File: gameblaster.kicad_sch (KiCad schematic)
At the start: 67 parts, among them IC1 TEA2025, IC10 74LS138, IC11 74LS08, IC12 74LS14, IC2 SAA1099, IC3 SAA1099, IC4 74LS374, IC5 74LS138, IC6 74LS74, IC7 74LS245, IC8 74LS32, IC9 74LS125, J1 Conn_02x06_Odd_Even

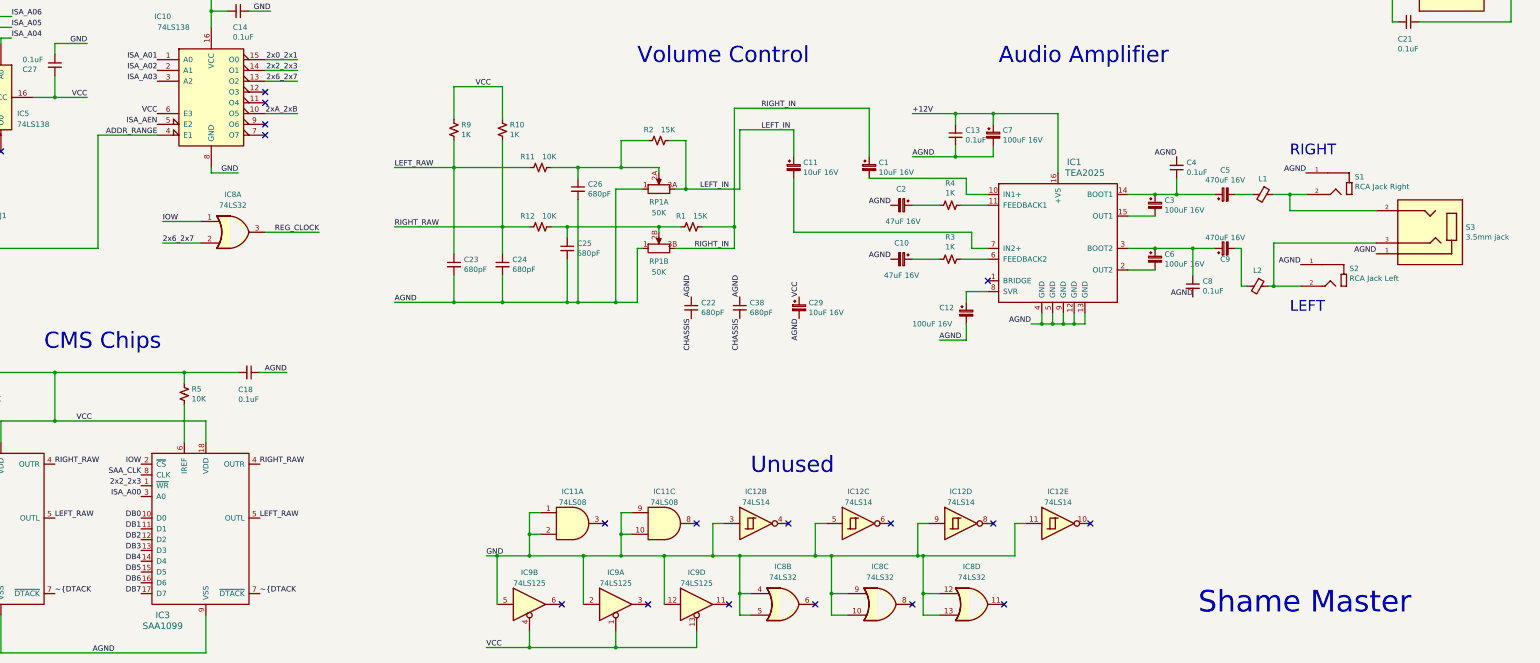
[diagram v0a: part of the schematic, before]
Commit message: add zener regulator for SAA1099s
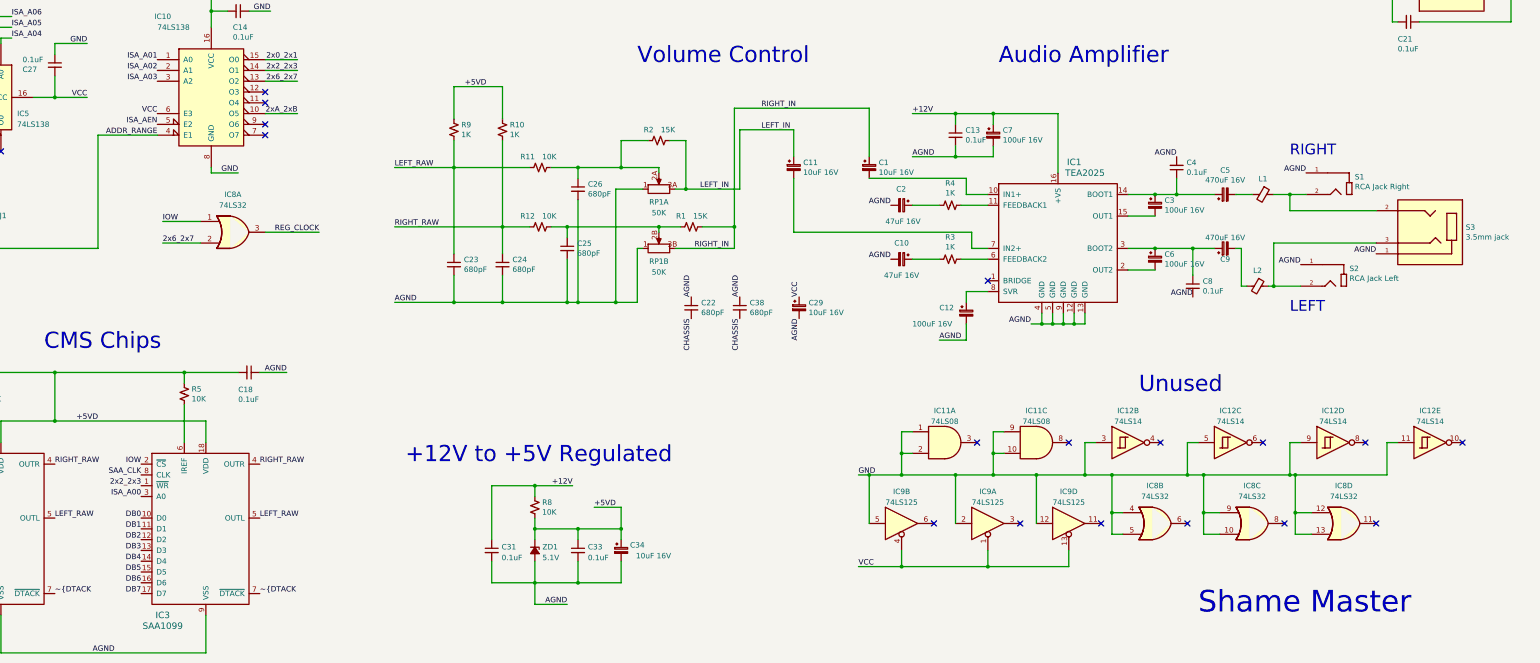
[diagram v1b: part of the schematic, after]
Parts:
- added C31, C33: 0.1uF, gameblaster:CAPAC200, symbol Device:C_Small
- added C34: 10uF 16V, gameblaster:CAPAP100, symbol gameblaster-rescue:CP_Small-Device
- added R8: 10K, gameblaster:RESA400, symbol Device:R_Small_US
- added ZD1: 5.1V, gameblaster:DIOA400, symbol Device:D_Zener_Small_Filled
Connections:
- net +12V: now also C31.1, R8.1
- net AGND: now also C31.2, C33.2, C34.2, ZD1.2 (A)
- net VCC: no longer C18.2, C19.1, IC2.18 (VDD), IC3.18 (VDD), R10.1, R5.1, R7.1, R9.1
- new net +5VD: C18.2, C19.1, C33.1, C34.1, IC2.18 (VDD), IC3.18 (VDD), R10.1, R5.1, R7.1, R8.2, R9.1, ZD1.1 (K)
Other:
- note added: "+12V to +5V Regulated"
- moved on the sheet: IC11A, IC11C, IC12B, IC12C, IC12D, IC12E, IC8B, IC8C, IC8D, IC9A, IC9B, IC9D

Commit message: add logo, engorge zones, clip solder mask from card fingers
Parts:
- S2: footprint gameblaster:CUI_RCJ-042 -> gameblaster:CUI_RCJ-043
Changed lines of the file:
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@@
       (effects (font (size 1.27 1.27)) (justify right))
     )
-    (property "Footprint" "gameblaster:CUI_RCJ-042" (id 2) (at 355.6 184.15 0)
+    (property "Footprint" "gameblaster:CUI_RCJ-043" (id 2) (at 355.6 184.15 0)
       (effects (font (size 1.27 1.27)) hide)
     )
@@
     )
     (path "/00000000-0000-0000-0000-000063df565c"
-      (reference "S2") (unit 1) (value "RCA Jack Left") (footprint "gameblaster:CUI_RCJ-042")
+      (reference "S2") (unit 1) (value "RCA Jack Left") (footprint "gameblaster:CUI_RCJ-043")
     )
     (path "/00000000-0000-0000-0000-000063df6ee7"

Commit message: so much dumb shit
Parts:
- removed C17: 0.1uF, gameblaster:CAPAC200, symbol gameblaster-rescue:C_Small-Adlib-cache
- removed C23, C24: 680pF, gameblaster:CAPAC200, symbol gameblaster-rescue:C_Small-Adlib-cache
- removed IC12: 74LS14, gameblaster:DIP254P762X635-14, symbol 74xx:74LS14
- removed R10, R9: 1K, gameblaster:RESA400, symbol Device:R_Small_US
- added C35: 0.1uF?, gameblaster:CAPAC200, symbol Device:C_Small
- added C? (x2): 1uF tant, gameblaster:CAPAP100, symbol Device:C_Polarized_Small
- added R?: 10K, gameblaster:RESA400, symbol Device:R_Small_US
- C10, C2: value 47uF 16V -> 22uF 16V
- R6: value 4.7K -> 1K
- R8: value 10K -> 470R
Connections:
- net +12V: no longer C13.1, C7.1, IC1.16 (+VS)
- net GND: now also C35.2, R?.2; no longer IC11.1, IC11.2, IC9.2, IC9.5
- net ISA_RST: now also C37.2, IC9.4
- net LEFT_IN: now also C11.2, RP1.2A; no longer C11.1, RP1.3A
- net RIGHT_IN: now also C1.2, RP1.2B; no longer C1.1, RP1.3B
- net VCC: now also IC11.1, IC9.2; no longer C37.2, IC9.1, IC9.4
- net ~{DTACK}: now also IC9.5; no longer IC11.4
- net ~{2x6_2x7}: now reaches IC10.12 (O3)
- net ~{2x6_2x7}: now also IC8.2
- net at IC1.10 (IN1+): now also C1.1; no longer C1.2
- net at IC1.7 (IN2+): now also C11.1; no longer C11.2
- net at C26.1, R11.2: now also C?.1; no longer R2.1, RP1.2A
- net at C25.1, R12.2: now also C?.1; no longer R1.1, RP1.2B
- net at IC6.10 (~{S}): now also IC9.6; no longer IC11.6
- net at IC6.11 (C): now also IC9.3, R?.1
- net ~{SAA_IOW}: now reaches IC11.3
- net ~{SAA_IOW}: now also IC2.1 (~{WR}), IC3.1 (~{WR}), C35.1
- net +5VD renamed +5VA
- net +5VA: now also C13.1, C7.1, IC1.16 (+VS)
- net 2x0_2x1 renamed ~{2x0_2x1}
- net ~{2x0_2x1}: now also IC11.12, IC2.2 (~{CS}); no longer IC2.1 (~{WR})
- net 2x2_2x3 renamed ~{2x2_2x3}
- net ~{2x2_2x3}: now also IC11.13, IC3.2 (~{CS}); no longer IC3.1 (~{WR})
- removed net 2x6_2x7: IC10.13 (O2), IC11.12, IC8.2
- net 2xA_2xB renamed ~{2xA_2xB}
- net ~{2xA_2xB}: no longer IC11.13
- net ADDR_RANGE renamed ~{ADDR_RANGE}
- net IOR renamed ~{IOR}
- net IOW renamed ~{IOW}
- net ~{IOW}: now also IC11.2, IC9.1; no longer IC2.2 (~{CS}), IC3.2 (~{CS})
- net REG_CLOCK renamed ~{REG_CLOCK}
- net ~{RESET}: no longer names the net of IC11.5
- new net: C?.2, R1.1, RP1.3B
- new net: C?.2, R2.1, RP1.3A
- new net ~{7FH_READ}: IC10.13 (O2)
- no-connect marks 52 -> 45
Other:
- note added: "(Leave RP1 unpopulated and replace R1 and R2 with 4.7K resistors for a fixed "medium" volume)"
- note added: "Write Logic"
- moved on the sheet: C1, C11, C20, C25, C26, C28, C37, IC11A, IC11B, IC11D, IC4, IC6A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

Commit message: dumb schematic shit
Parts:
- gave numbers to parts that had none: 3
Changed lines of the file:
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@@
   (symbol (lib_id "Device:C_Polarized_Small") (at 181.61 172.72 90) (unit 1)
     (in_bom yes) (on_board yes) (fields_autoplaced)
-    (property "Reference" "C?" (id 0) (at 181.0639 167.6232 90))
+    (property "Reference" "C23" (id 0) (at 181.0639 167.6232 90))
     (property "Value" "1uF tant" (id 1) (at 181.0639 170.1601 90))
     (property "Footprint" "gameblaster:CAPAP100" (id 2) (at 181.61 172.72 0)
@@
   (symbol (lib_id "Device:C_Polarized_Small") (at 181.61 158.75 90) (unit 1)
     (in_bom yes) (on_board yes) (fields_autoplaced)
-    (property "Reference" "C?" (id 0) (at 181.0639 153.6532 90))
+    (property "Reference" "C17" (id 0) (at 181.0639 153.6532 90))
     (property "Value" "1uF tant" (id 1) (at 181.0639 156.1901 90))
     (property "Footprint" "gameblaster:CAPAP100" (id 2) (at 181.61 158.75 0)
@@
   (symbol (lib_id "Device:R_Small_US") (at 218.44 78.74 0) (unit 1)
     (in_bom yes) (on_board yes)
-    (property "Reference" "R?" (id 0) (at 220.98 77.47 0))
+    (property "Reference" "R9" (id 0) (at 220.98 77.47 0))
     (property "Value" "10K" (id 1) (at 219.71 80.01 0)
       (effects (font (size 1.27 1.27)) (justify left))
@@
       (reference "C16") (unit 1) (value "0.1uF") (footprint "gameblaster:CAPAC200")
     )
+    (path "/c08901b8-33b1-4c09-abd5-c90fae277cfd"
+      (reference "C17") (unit 1) (value "1uF tant") (footprint "gameblaster:CAPAP100")
+    )
     (path "/00000000-0000-0000-0000-000063e0a803"
       (reference "C18") (unit 1) (value "0.1uF") (footprint "gameblaster:CAPAC200")
@@
       (reference "C22") (unit 1) (value "680pF") (footprint "gameblaster:CAPAC200")
     )
+    (path "/04e1ceed-18cf-4d16-a60e-8b84fb42586e"
+      (reference "C23") (unit 1) (value "1uF tant") (footprint "gameblaster:CAPAP100")
+    )
     (path "/00000000-0000-0000-0000-00006403d753"
       (reference "C25") (unit 1) (value "680pF") (footprint "gameblaster:CAPAC200")
@@
       (reference "C38") (unit 1) (value "680pF") (footprint "gameblaster:CAPAC200")
     )
-    (path "/04e1ceed-18cf-4d16-a60e-8b84fb42586e"
-      (reference "C?") (unit 1) (value "1uF tant") (footprint "gameblaster:CAPAP100")
-    )
-    (path "/c08901b8-33b1-4c09-abd5-c90fae277cfd"
-      (reference "C?") (unit 1) (value "1uF tant") (footprint "gameblaster:CAPAP100")
-    )
     (path "/00000000-0000-0000-0000-000063e2477d"
       (reference "F1") (unit 1) (value "MountingHole") (footprint "gameblaster:MNT_KEYSTONE_9202")
@@
       (reference "R8") (unit 1) (value "470R") (footprint "gameblaster:RESA400")
     )
+    (path "/de5081d7-c9ca-401c-b128-a39de91cb81e"
+      (reference "R9") (unit 1) (value "10K") (footprint "gameblaster:RESA400")
+    )
     (path "/00000000-0000-0000-0000-000063dfd8aa"
       (reference "R11") (unit 1) (value "10K") (footprint "gameblaster:RESA400")
@@
       (reference "R19") (unit 1) (value "4.7K") (footprint "gameblaster:RESA400")
     )
-    (path "/de5081d7-c9ca-401c-b128-a39de91cb81e"
-      (reference "R?") (unit 1) (value "10K") (footprint "gameblaster:RESA400")
-    )
     (path "/1bd276f5-593a-4fdb-b158-a8c28f21f786"

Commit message: heavily annotate schematic
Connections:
- net AGND: now also C38.2; no longer C38.1
- net CHASSIS: now also C38.1; no longer C38.2
- net GND: now also IC11.4, IC11.5
- net ISA_IO_CH_RDY renamed ~{IORDY}
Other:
- note added: ""EMI" "Protection""
- note added: "+5V is low for a TEA2025B, but apparently still in operating range. (The Sound Blaster used a 12V -> 9V regulator, but the Game Blaster just used this zener-regulated 12V -> 5V circuit for all the analog power)"
- note added: "- ~{CS} goes low -> ~{WR} goes low - register 0/1 (control/data) selected by A0 - SAA1099 latches data from D0-D7 into register - SAA1099 pulls ~{DTACK} low when data trasnfer is complete"
- note added: "210"
- note added: "220"
- note added: "230"
- note added: "240"
- note added: "250"
- note added: "260"
- note added: "2x0h through 2x3h are ~{CS} for the SAA1099s; selecting either puts a 0 onto Data for the flip flop, and writing to it clocks the data to the buffer. When a write happens, the buffer control pin goes low, pulling IO_CH_READY on the ISA bus low, introducing a wait state."
- note added: "As long as the ISA bus isn't reset, the pull-up drives ~{Pre-set} on the flip flop high/inactive. When the SAA1099 finishes a read cycle, it drives ~{DTACK} low, which drives ~{Pre-set} active, enabling the buffer to pull ~{IORDY} low, finishing the wait- state."
- note added: "Aww yeah we coupling"
- note added: "Base Address - 210h to 260h"
- note added: "Because ~{CS} is already guaranteeing we're accessing this specific SAA1099, we just use the A0 line of the ISA bus directly to determine which register to write to."
- note added: "Bus transceivers are apparently good practice, so we take the ISA data bus D0-D7 and hook it up to a 74LS245 here. When ~{IOR} is pulled low (i.e. when we're reading from 2xA/2xBh or 2x4h on this card) we drive its direction pin to do B->A; otherwise, we're writing, and we run it A->B. ~{CE} is controlled by the output of the first decoder, which is low when an address within our base port range 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"
- note added: "Hey, look! It's a 23.417KHz RC low-pass filter! The SAA1099 clicks and pops something fierce when it powers on, so this is likely here to protect whatever audio equipment is plugged into it."
- note added: "ISA Bus clock is 14.318MHz, nominal SAA1099 clock is about 8MHz, the Game Blaster runs the SAA1099s at 7.159MHz by dividing the ISA clock in half."
- note added: "Now we're REALLY coupled"
- note added: "Since we want to save the contents of the bus into the detection register when a write is made to 2x6h or 2x7h, we clock the 74LS374 when ~{IOW} and ~{2x6_2x7} are both low. (i.e. when the host indicates a write, and when the address selected is the "ID write" port)"
- note added: "The original Game Blaster includes this AND of VCC and ~{IOW} to drive ~{WR} on the SAA1099, I suspect because the timing diagrams on the SAA1099 datasheet require that ~{WR} goes low slightly after ~{CS} goes low to start the data transfer. (Are these caps here to add delay? How do capacitors work?)"
- note added: "The original Game Blaster uses a tantalum for the polarized cap here, and has a couple extra 0.1uF caps in the circuit. This circuit is lifted from the Sound Blaster."
- note added: "This is only capable of decoding addresses in pairs, which is fine because the SAA1099s each have two registers. 2x0-2x1h are the left SAA1099, 2x2-2x3h are the right SAA1099. 2x4 is used on the original card to read back a status bit from the DIP-40, but conventional wisdom says "just read 7Fh". Card detection requires accepting a write to 2x6h (or 2x7h), and reading the same value back on 2xAh 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"
- note added: "We use a 74LS374 octal flip-flop as a register to store the value written to 2x6/2x7h, and read it back on 2xA/2xBh, by putting DB0-DB7 on both the input and output. ~{REG_CLOCK} is the AND of ~{IOW} and ~{2x6_2x7}, which means that we latch data into the register when we write there. ~{OE} is controlled by ~{2xA_2xB}, so that when we read from those ports, the outputs are placed onto the transce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"
- moved on the sheet: BUS1, C1, C10, C11, C12, C13, C14, C15, C16, C17, C18, C19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

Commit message: Separate +5VA and VDDA; re-add SAA1099 output current source; use power symbols
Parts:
- added C24, C36: 680pF, gameblaster:CAPAC200, symbol gameblaster-rescue:C_Small-Adlib-cache
- added R10, R13: 1.5K, gameblaster:RESA400, symbol Device:R_Small_US
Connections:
- net +5VA: now also BUS1.1 (GND), C10.2, C12.2, C13.2, C18.1, C19.2, C22.1, C25.2, C26.2, C29.2, C31.2, C33.2, C34.2, C37.1, C38.2, C4.1, C7.2, C8.2, IC1.12 (GND), IC1.13 (GND), IC1.4 (GND), IC1.5 (GND), IC1.9 (GND), IC2.9 (VSS), IC3.9 (VSS), RP1.1, RP1.1, S1.1, S2.1, S3.1, ZD1.2 (A), C24.2, C36.2; no longer C33.1, C34.1, R5.1, R7.1, R8.2, ZD1.1 (K)
- net GND: no longer BUS1.1 (GND), BUS1.10 (GND), C37.1
- net LEFT_RAW: now also C36.1, R13.1
- net RIGHT_RAW: now also C24.1, R10.1
- net VCC: no longer BUS1.3 (VCC), C29.1
- net at C3.1, C5.1, IC1.14 (BOOT1): now also C4.2; no longer C4.1
- removed net AGND: C10.2, C12.2, C13.2, C18.1, C19.2, C2.2, C22.1, C25.2, C26.2, C29.2, C31.2, C33.2, C34.2, C38.2, C4.2, C7.2, C8.2, IC1.12 (GND), IC1.13 (GND), IC1.4 (GND), IC1.5 (GND), IC1.9 (GND), IC2.9 (VSS), IC3.9 (VSS), RP1.1, RP1.1, S1.1, S2.1, S3.1, ZD1.2 (A)
- new net: BUS1.3 (VCC), C29.1
- new net VDDA: C33.1, C34.1, R10.2, R13.2, R5.1, R7.1, R8.2, ZD1.1 (K)
- no-connect marks 45 -> 46
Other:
- note added: "Hey, look! It's a 23.417KHz RC low-pass filter!"
- note removed: "Hey, look! It's a 23.417KHz RC low-pass filter! The SAA1099 clicks and pops something fierce when it powers on, so this is likely here to protect whatever audio equipment is plugged into it."
- moved on the sheet: C1, C10, C11, C12, C13, C17, C18, C19, C2, C23, C25, C26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

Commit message: updated board
yes i know the left ICs are misaligned
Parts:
- C1, C11: value 10uF 16V -> 0.22uF 16V
- renumbered IC6 to IC12, IC7 to IC4, IC4 to IC5, IC5 to IC6, IC10 to IC7
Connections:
- net +5VA: now also BUS1.3 (VCC), C29.1; no longer BUS1.1 (GND), C10.2, C12.2, C13.2, C18.1, C19.1, C22.1, C24.2, C25.2, C26.2, C29.2, C31.2, C33.2, C34.2, C36.2, C37.1, C38.2, C4.1, C7.2, C8.2, IC1.12 (GND), IC1.13 (GND), IC1.4 (GND), IC1.5 (GND), IC1.9 (GND), IC2.9 (VSS), IC3.9 (VSS), RP1.1, RP1.1, S1.1, S2.1, S3.1, ZD1.2 (A)
- net CHASSIS: now also C38.2; no longer C38.1
- net GNDREF: now reaches C2.2
- net GNDREF: now also BUS1.1 (GND), C10.2, C12.2, C13.2, C18.1, C19.1, C22.1, C24.2, C25.2, C26.2, C29.2, C31.2, C33.2, C34.2, C36.2, C37.1, C38.1, C4.1, C7.2, C8.2, IC1.12 (GND), IC1.13 (GND), IC1.4 (GND), IC1.5 (GND), IC1.9 (GND), IC2.9 (VSS), IC3.9 (VSS), RP1.1, RP1.1, S1.1, S2.1, S3.1, ZD1.2 (A)
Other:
- moved on the sheet: C29, C38
